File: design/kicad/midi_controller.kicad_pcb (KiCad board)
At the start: 4 copper layers, 166 x 166 mm, 30 parts, among them J1 Conn_01x02_Socket, J2 Conn_01x02_Socket, J3 Conn_01x02_Socket, J4 Conn_01x02_Socket, J5 Conn_01x02_Socket, J6 Conn_01x02_Socket, J7 Conn_01x05, U1 CD74HC4067M

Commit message: Add schematic for MIDI Display MSP2807 with associated components
- Created a new schematic file for the MIDI Display MSP2807.
- Included a unpolarized capacitor (C2) with a value of 100nF.
- Added properties such as reference, value, footprint, and datasheet for the capacitor.
- Integrated the MIDI Display module with detailed pin configurations and properties.
- Defined hierarchical labels for power and data connections (VCC, GND, CS, RST, DC, etc.).
- Ensured all components are marked for BOM inclusion and simulation.
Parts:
- added C5: 10u, Capacitor_SMD:C_0805_2012Metric, F.Cu at (149.9, 21.6)
- added C6: 100n, Capacitor_SMD:C_0603_1608Metric, F.Cu at (154.2, 21.4)
- added C7: 100n, Capacitor_SMD:C_0603_1608Metric, F.Cu at (154.2, 23.9)
- added C8: 10u, Capacitor_SMD:C_0805_2012Metric, F.Cu at (149.9, 24.6)
- added D10: PESD5V0L1BA,115, KiCad:SOD2512X110N, F.Cu at (125.6, 46.6)
- added D11: PESD5V0L1BA,115, KiCad:SOD2512X110N, F.Cu at (125.6, 50.0)
- added D12: PESD5V0L1BA,115, KiCad:SOD2512X110N, F.Cu at (125.6, 53.3)
- added D13: PESD5V0L1BA,115, KiCad:SOD2512X110N, F.Cu at (132.6, 34.6)
- added D14: PESD5V0L1BA,115, KiCad:SOD2512X110N, F.Cu at (132.6, 37.9)
- added D15: PESD5V0L1BA,115, KiCad:SOD2512X110N, F.Cu at (132.6, 41.3)
- added D16: PESD5V0L1BA,115, KiCad:SOD2512X110N, F.Cu at (139.6, 34.6)
- added D17: PESD5V0L1BA,115, KiCad:SOD2512X110N, F.Cu at (139.6, 37.9)
- added D18: PESD5V0L1BA,115, KiCad:SOD2512X110N, F.Cu at (139.6, 41.3)
- added D19: PESD5V0L1BA,115, KiCad:SOD2512X110N, F.Cu at (142.7, 20.5)
- added D2: SS34, Diode_SMD:D_SMA, F.Cu at (127.1, 12.7)
- added D20: PESD5V0L1BA,115, KiCad:SOD2512X110N, F.Cu at (142.7, 23.9)
- added D21: PESD5V0L1BA,115, KiCad:SOD2512X110N, F.Cu at (142.7, 27.2)
- added D22: PESD5V0L1BA,115, KiCad:SOD2512X110N, F.Cu at (125.6, 34.6)
- added D23: PESD5V0L1BA,115, KiCad:SOD2512X110N, F.Cu at (125.6, 37.9)
- added D24: PESD5V0L1BA,115, KiCad:SOD2512X110N, F.Cu at (125.6, 41.3)
- added D25: PESD5V0L1BA,115, KiCad:SOD2512X110N, F.Cu at (139.6, 46.6)
- added D26: PESD5V0L1BA,115, KiCad:SOD2512X110N, F.Cu at (139.6, 50.0)
- added D27: PESD5V0L1BA,115, KiCad:SOD2512X110N, F.Cu at (139.6, 53.3)
- added D28: PESD5V0L1BA,115, KiCad:SOD2512X110N, F.Cu at (118.6, 42.6)
- added D29: PESD5V0L1BA,115, KiCad:SOD2512X110N, F.Cu at (118.6, 46.0)
- added D3: SMAJ5.0CA, Diode_SMD:D_SMA, F.Cu at (135.6, 7.11)
- added D30: PESD5V0L1BA,115, KiCad:SOD2512X110N, F.Cu at (118.6, 49.3)
- added D31: PESD5V0L1BA,115, KiCad:SOD2512X110N, F.Cu at (118.6, 20.5)
- added D32: PESD5V0L1BA,115, KiCad:SOD2512X110N, F.Cu at (118.6, 23.9)
- added D33: PESD5V0L1BA,115, KiCad:SOD2512X110N, F.Cu at (118.6, 27.2)
- added D34: PESD5V0L1BA,115, KiCad:SOD2512X110N, F.Cu at (118.6, 30.6)
- added D35: PESD5V0L1BA,115, KiCad:SOD2512X110N, F.Cu at (118.6, 33.9)
- added D36: PESD5V0L1BA,115, KiCad:SOD2512X110N, F.Cu at (118.6, 37.3)
- added D37: PESD5V0L1BA,115, KiCad:SOD2512X110N, F.Cu at (150.7, 32.6)
- added D38: PESD5V0L1BA,115, KiCad:SOD2512X110N, F.Cu at (150.7, 36.0)
- added D39: PESD5V0L1BA,115, KiCad:SOD2512X110N, F.Cu at (150.7, 39.3)
- added D4: PESD5V0L1BA,115, KiCad:SOD2512X110N, F.Cu at (132.6, 46.6)
- added D40: PESD5V0L1BA,115, KiCad:SOD2512X110N, F.Cu at (150.7, 42.7)
- added D5: PESD5V0L1BA,115, KiCad:SOD2512X110N, F.Cu at (132.6, 50.0)
- added D6: PESD5V0L1BA,115, KiCad:SOD2512X110N, F.Cu at (132.6, 53.3)
- added D7: PESD5V0L1BA,115, KiCad:SOD2512X110N, F.Cu at (135.7, 20.5)
- added D8: PESD5V0L1BA,115, KiCad:SOD2512X110N, F.Cu at (135.7, 23.9)
- added D9: PESD5V0L1BA,115, KiCad:SOD2512X110N, F.Cu at (135.7, 27.2)
- added F1: Fuse, Fuse:Fuse_0805_2012Metric, F.Cu at (125.3, 29.4)
- C1: renamed from C2; footprint Capacitor_SMD:C_0805_2012Metric -> Capacitor_SMD:C_0603_1608Metric
- renumbered C1 to C2, J7 to J1, J1 to J2, J2 to J3, J3 to J4, J4 to J5, J5 to J6, J6 to J7
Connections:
- MCU1 pad 48: +5V -> Net-(MCU1-VIN)

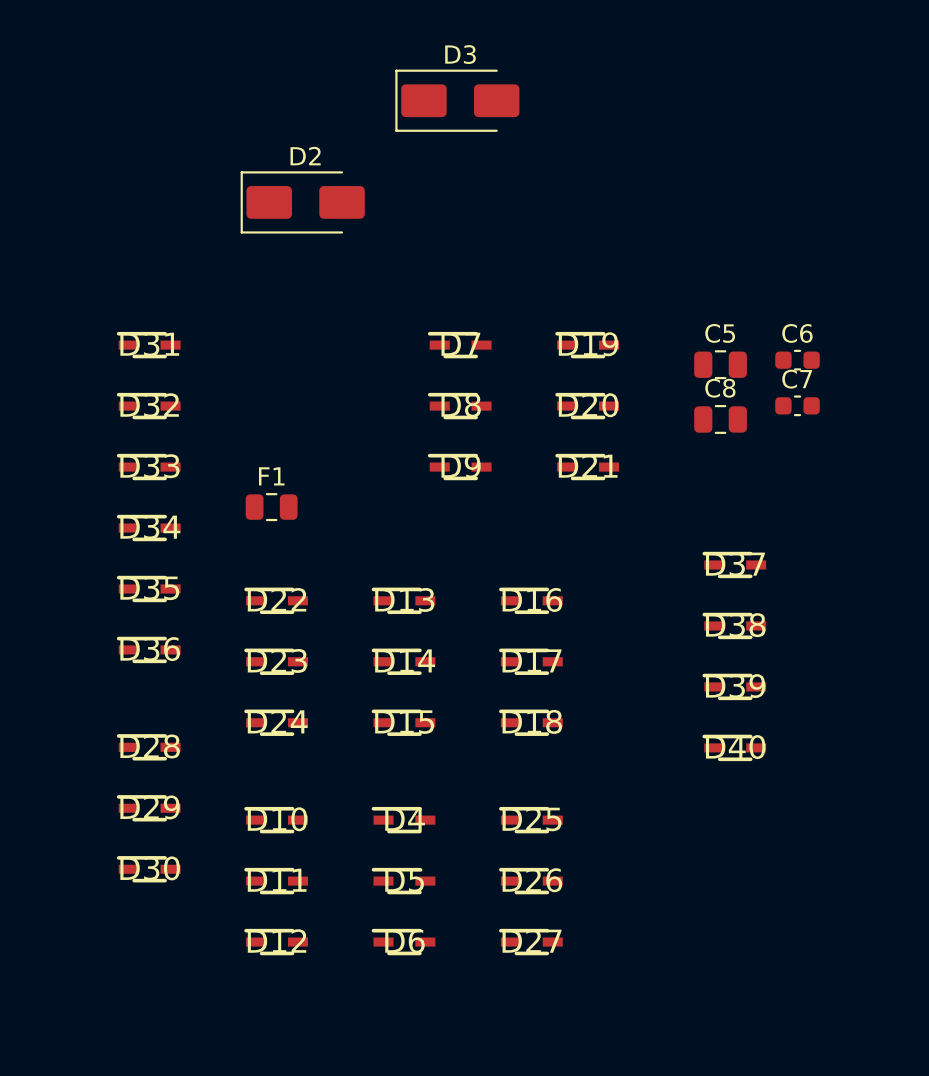
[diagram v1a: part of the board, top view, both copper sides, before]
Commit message: Fix reference labels and update wire connections in MIDI controller and multiplexer schematics
- Adjusted wire connection points in the MIDI controller schematic for better alignment.
- Updated label positions for various components in the MIDI controller schematic.
- Renamed reference designators for capacitors and power connections in the multiplexer schematic to maintain consistency.
- Corrected the reference designators for multiple components to reflect accurate labeling.
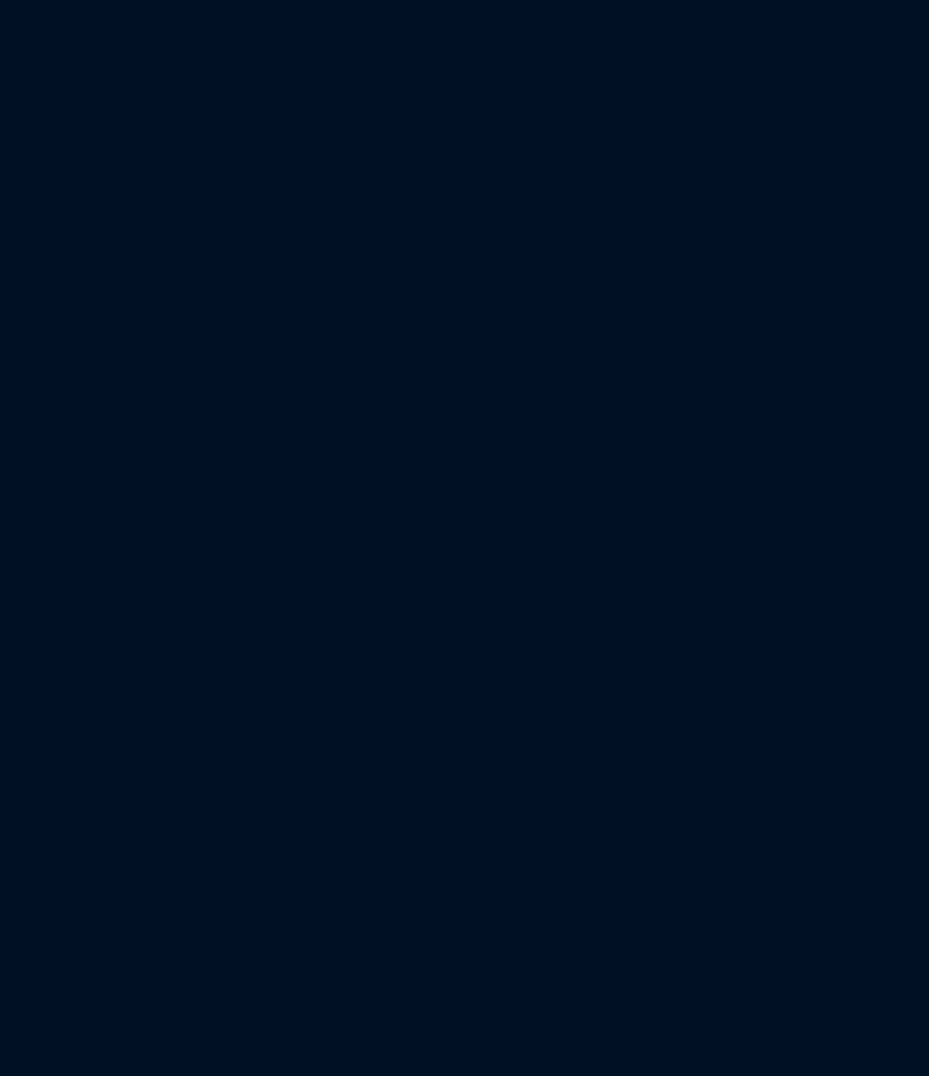
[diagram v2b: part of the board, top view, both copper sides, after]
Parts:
- removed C5, C8: 10u, Capacitor_SMD:C_0805_2012Metric
- removed C6, C7: 100n, Capacitor_SMD:C_0603_1608Metric
- removed D10, D11, D12, D13, D14, D15, D16, D17, D18, D19, D20, D21, D22, D23, D24, D25, D26, D27, D28, D29, D30, D31, D32, D33, D34, D35, D36, D37, D38, D39, D4, D40, D5, D6, D7, D8, D9: PESD5V0L1BA,115, KiCad:SOD2512X110N
- removed D2: SS34, Diode_SMD:D_SMA
- removed D3: SMAJ5.0CA, Diode_SMD:D_SMA
- removed F1: Fuse, Fuse:Fuse_0805_2012Metric

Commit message: Update kicad binary files
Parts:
- added C1: 100p, Capacitor_SMD:C_0603_1608Metric, F.Cu at (33.7, -58.7)
- added C10: 47u, Capacitor_SMD:C_1206_3216Metric, F.Cu at (51.1, -58.3)
- added C11: 47u, Capacitor_SMD:C_1206_3216Metric, F.Cu at (51.1, -54.9)
- added C12: 100u, Capacitor_SMD:C_1210_3225Metric, F.Cu at (39.0, -45.3)
- added C13: 100n, Capacitor_SMD:C_0603_1608Metric, F.Cu at (62.9, -22.5)
- added C14: 100n, Capacitor_SMD:C_0603_1608Metric, F.Cu at (62.9, -20.0)
- added C15: 100n, Capacitor_SMD:C_0603_1608Metric, F.Cu at (62.9, -17.5)
- added C16: 100n, Capacitor_SMD:C_0603_1608Metric, F.Cu at (45.7, -21.2)
- added C17: 100n, Capacitor_SMD:C_0603_1608Metric, F.Cu at (45.7, -18.7)
- added C18: 100n, Capacitor_SMD:C_0603_1608Metric, F.Cu at (45.7, -16.2)
- added C19: 100n, Capacitor_SMD:C_0603_1608Metric, F.Cu at (62.9, -46.6)
- added C2: 10u, Capacitor_SMD:C_0805_2012Metric, F.Cu at (33.9, -45.9)
- added C20: 100n, Capacitor_SMD:C_0603_1608Metric, F.Cu at (62.9, -44.1)
- added C21: 100n, Capacitor_SMD:C_0603_1608Metric, F.Cu at (62.9, -41.6)
- added C22: 100n, Capacitor_SMD:C_0603_1608Metric, F.Cu at (73.9, -46.6)
- added C23: 100n, Capacitor_SMD:C_0603_1608Metric, F.Cu at (73.9, -44.1)
- added C24: 100n, Capacitor_SMD:C_0603_1608Metric, F.Cu at (73.9, -41.6)
- added C25: 100n, Capacitor_SMD:C_0603_1608Metric, F.Cu at (62.9, -34.6)
- added C26: 100n, Capacitor_SMD:C_0603_1608Metric, F.Cu at (62.9, -32.1)
- added C27: 100n, Capacitor_SMD:C_0603_1608Metric, F.Cu at (62.9, -29.6)
- added C28: 100n, Capacitor_SMD:C_0603_1608Metric, F.Cu at (62.9, -58.7)
- added C29: 100n, Capacitor_SMD:C_0603_1608Metric, F.Cu at (62.9, -56.2)
- added C3: 100n, Capacitor_SMD:C_0603_1608Metric, F.Cu at (33.7, -56.2)
- added C30: 100n, Capacitor_SMD:C_0603_1608Metric, F.Cu at (62.9, -53.7)
- added C31: 100n, Capacitor_SMD:C_0603_1608Metric, F.Cu at (73.9, -58.7)
- added C32: 100n, Capacitor_SMD:C_0603_1608Metric, F.Cu at (73.9, -56.2)
- added C33: 100n, Capacitor_SMD:C_0603_1608Metric, F.Cu at (73.9, -53.7)
- added C34: 100n, Capacitor_SMD:C_0603_1608Metric, F.Cu at (73.9, -34.6)
- added C35: 100n, Capacitor_SMD:C_0603_1608Metric, F.Cu at (73.9, -32.1)
- added C36: 100n, Capacitor_SMD:C_0603_1608Metric, F.Cu at (73.9, -29.6)
- added C37: 100n, Capacitor_SMD:C_0603_1608Metric, F.Cu at (73.9, -22.5)
- added C38: 100n, Capacitor_SMD:C_0603_1608Metric, F.Cu at (73.9, -20.0)
- added C39: 100n, Capacitor_SMD:C_0603_1608Metric, F.Cu at (73.9, -17.5)
- added C41: 10uF_0805_16V_lowESR, Capacitor_SMD:C_0805_2012Metric, F.Cu at (80.2, -22.3)
- added C43: 10u, Capacitor_SMD:C_0805_2012Metric, F.Cu at (45.9, -36.3)
- added C5: 1n, Capacitor_SMD:C_0603_1608Metric, F.Cu at (33.7, -53.7)
- added C6: 10n, Capacitor_SMD:C_0603_1608Metric, F.Cu at (33.7, -51.2)
- added C7: 1n, Capacitor_SMD:C_0603_1608Metric, F.Cu at (33.7, -48.7)
- added C9: 100n, Capacitor_SMD:C_0805_2012Metric, F.Cu at (33.9, -42.9)
- added D1: SS34, Diode_SMD:D_SMA, F.Cu at (47.8, -46.7)
- added D10: PESD5V0L1BA,115, KiCad:SOD2512X110N, F.Cu at (58.4, -42.9)
- added D11: PESD5V0L1BA,115, KiCad:SOD2512X110N, F.Cu at (58.4, -39.5)
- added D12: PESD5V0L1BA,115, KiCad:SOD2512X110N, F.Cu at (69.4, -46.2)
- added D13: PESD5V0L1BA,115, KiCad:SOD2512X110N, F.Cu at (69.4, -42.9)
- added D14: PESD5V0L1BA,115, KiCad:SOD2512X110N, F.Cu at (69.4, -39.5)
- added D15: PESD5V0L1BA,115, KiCad:SOD2512X110N, F.Cu at (58.4, -34.2)
- added D16: PESD5V0L1BA,115, KiCad:SOD2512X110N, F.Cu at (58.4, -30.8)
- added D17: PESD5V0L1BA,115, KiCad:SOD2512X110N, F.Cu at (58.4, -27.5)
- added D18: PESD5V0L1BA,115, KiCad:SOD2512X110N, F.Cu at (58.4, -58.3)
- added D19: PESD5V0L1BA,115, KiCad:SOD2512X110N, F.Cu at (58.4, -54.9)
- added D2: SMAJ5.0CA, Diode_SMD:D_SMA, F.Cu at (47.8, -42.1)
- added D20: PESD5V0L1BA,115, KiCad:SOD2512X110N, F.Cu at (58.4, -51.6)
- added D21: PESD5V0L1BA,115, KiCad:SOD2512X110N, F.Cu at (69.4, -58.3)
- added D22: PESD5V0L1BA,115, KiCad:SOD2512X110N, F.Cu at (69.4, -54.9)
- added D23: PESD5V0L1BA,115, KiCad:SOD2512X110N, F.Cu at (69.4, -51.6)
- added D24: PESD5V0L1BA,115, KiCad:SOD2512X110N, F.Cu at (69.4, -34.2)
- added D25: PESD5V0L1BA,115, KiCad:SOD2512X110N, F.Cu at (69.4, -30.8)
- added D26: PESD5V0L1BA,115, KiCad:SOD2512X110N, F.Cu at (69.4, -27.5)
- added D27: PESD5V0L1BA,115, KiCad:SOD2512X110N, F.Cu at (69.4, -22.1)
- added D28: PESD5V0L1BA,115, KiCad:SOD2512X110N, F.Cu at (69.4, -18.8)
- added D29: PESD5V0L1BA,115, KiCad:SOD2512X110N, F.Cu at (69.4, -15.4)
- added D3: PESD5V0L1BA,115, KiCad:SOD2512X110N, F.Cu at (58.4, -22.1)
- added D30: PESD5V0L1BA,115, KiCad:SOD2512X110N, F.Cu at (34.2, -36.2)
- added D31: PESD5V0L1BA,115, KiCad:SOD2512X110N, F.Cu at (34.2, -32.8)
- added D32: PESD5V0L1BA,115, KiCad:SOD2512X110N, F.Cu at (34.2, -29.5)
- added D33: PESD5V0L1BA,115, KiCad:SOD2512X110N, F.Cu at (34.2, -26.1)
- added D34: PESD5V0L1BA,115, KiCad:SOD2512X110N, F.Cu at (34.2, -22.8)
- added D35: PESD5V0L1BA,115, KiCad:SOD2512X110N, F.Cu at (34.2, -19.4)
- added D36: PESD5V0L1BA,115, KiCad:SOD2512X110N, F.Cu at (41.2, -36.2)
- added D37: PESD5V0L1BA,115, KiCad:SOD2512X110N, F.Cu at (41.2, -32.8)
- added D38: PESD5V0L1BA,115, KiCad:SOD2512X110N, F.Cu at (41.2, -29.5)
- added D39: PESD5V0L1BA,115, KiCad:SOD2512X110N, F.Cu at (41.2, -26.1)
- added D4: PESD5V0L1BA,115, KiCad:SOD2512X110N, F.Cu at (58.4, -18.8)
- added D5: PESD5V0L1BA,115, KiCad:SOD2512X110N, F.Cu at (58.4, -15.4)
- added D6: PESD5V0L1BA,115, KiCad:SOD2512X110N, F.Cu at (41.2, -20.8)
- added D7: PESD5V0L1BA,115, KiCad:SOD2512X110N, F.Cu at (41.2, -17.4)
- added D8: PESD5V0L1BA,115, KiCad:SOD2512X110N, F.Cu at (41.2, -14.1)
- added D9: PESD5V0L1BA,115, KiCad:SOD2512X110N, F.Cu at (58.4, -46.2)
- added F1: Fuse, Fuse:Fuse_0805_2012Metric, F.Cu at (38.3, -41.7)
- added FB1: FerriteBead, Inductor_SMD:L_0805_2012Metric, F.Cu at (46.0, -58.6)
- added FB2: FerriteBead, Inductor_SMD:L_0805_2012Metric, F.Cu at (46.0, -55.8)
- added FB3: FerriteBead, Inductor_SMD:L_0805_2012Metric, F.Cu at (46.0, -53.1)
- added FB4: FerriteBead, Inductor_SMD:L_0805_2012Metric, F.Cu at (46.0, -50.3)
- added J9: Conn_01x14, Connector_PinSocket_2.54mm:PinSocket_1x14_P2.54mm_Vertical, F.Cu at (113.8, 91.0)
- added R1: 220, Resistor_SMD:R_0603_1608Metric, F.Cu at (37.7, -58.7)
- added R2: 100, Resistor_SMD:R_0603_1608Metric, F.Cu at (37.7, -56.2)
- added R3: 100, Resistor_SMD:R_0603_1608Metric, F.Cu at (37.7, -53.7)
- added R4: 100, Resistor_SMD:R_0603_1608Metric, F.Cu at (37.7, -51.2)
- added R5: 33, Resistor_SMD:R_0603_1608Metric, F.Cu at (37.7, -48.7)
- added R6: 33, Resistor_SMD:R_0603_1608Metric, F.Cu at (41.7, -58.7)
- added R7: 100, Resistor_SMD:R_0603_1608Metric, F.Cu at (41.7, -56.2)
- added R8: 33, Resistor_SMD:R_0603_1608Metric, F.Cu at (41.7, -53.7)
- added R9: 33, Resistor_SMD:R_0603_1608Metric, F.Cu at (41.7, -51.2)
- C42: renamed from C4; footprint Capacitor_SMD:C_0805_2012Metric -> Capacitor_SMD:C_0603_1608Metric
- renumbered C1 to C4, C2 to C40, C3 to C8, D1 to DISP1
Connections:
- net /Encoder with Push Button_Navigation/QUAD_A renamed /Encoder_with_Push_Button_Navigation/QUAD_A
- net /Encoder with Push Button_Navigation/QUAD_B renamed /Encoder_with_Push_Button_Navigation/QUAD_B
- net /Encoder with Push Button_Navigation/SW_A renamed /Encoder_with_Push_Button_Navigation/SW_A
- net Net-(D1-RST) renamed /RST
- net Net-(D1-SDO/MISO) renamed /MISO
- C4 pad 1: +3V3 -> Net-(C4-Pad1)
- DISP1 pad 3: Net-(D1-CS) -> /CS
- DISP1 pad 5: Net-(D1-DC) -> /DC
- DISP1 pad 6: Net-(D1-SDI/MOSI) -> /MOSI
- DISP1 pad 7: Net-(D1-SCK) -> /Display MSP2807/SCK
- DISP1 pad 8: +3V3 -> /Display MSP2807/LED
- J1 pad 1: +5V -> Net-(J1-Pin_1)
- MCU1 pad 18: Net-(D1-SDI/MOSI) -> Net-(MCU1-26_A12_MOSI1)
- MCU1 pad 19: Net-(D1-SCK) -> Net-(MCU1-27_A13_SCK1)
- MCU1 pad 2: Net-(D1-DC) -> Net-(MCU1-0_RX1_CRX2_CS1)
- MCU1 pad 20: Net-(D1-CS) -> Net-(MCU1-28_RX7)
- MCU1 pad 46: +3V3 -> Net-(C4-Pad1)
- MCU1 pad 5: /S0 -> Net-(MCU1-3_LRCLK2)
- MCU1 pad 6: /S1 -> Net-(MCU1-4_BCLK2)
- MCU1 pad 7: /S2 -> Net-(MCU1-5_IN2)
- MCU1 pad 8: /S3 -> Net-(MCU1-6_OUT1D)
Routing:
- net (no net): track 0.00 -> 225.4 mm
- net Net-(D1-CS): track 70.9 -> 0.00 mm
- net Net-(D1-SCK): track 68.3 -> 0.00 mm
- net Net-(D1-SDI/MOSI): track 64.0 -> 0.00 mm
- net Net-(D1-DC): track 22.3 -> 0.00 mm

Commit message: Update kicad binary files
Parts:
- removed MCU1: MIDI_Teensy4.1, midi_controller:Teensy41
- added J10: Conn_01x24_Socket, Connector_PinSocket_2.54mm:PinSocket_1x24_P2.54mm_Vertical, B.Cu at (133.0, 115.1)
- D36, D37, D38, D39, R2, R3, R4, R7: moved to B.Cu
- J9: value Conn_01x14 -> Conn_01x24_Socket; footprint Connector_PinSocket_2.54mm:PinSocket_1x14_P2.54mm_Vertical -> Connector_PinSocket_2.54mm:PinSocket_1x24_P2.54mm_Vertical; moved to B.Cu
- moved FB4 269.9 mm to (213.9, 161.0), turned to 180 degrees
- moved C1 218.5 mm to (180.2, 103.4), turned to 90 degrees
- moved FB1 210.1 mm to (177.7, 105.2)
- moved R8 207.8 mm to (178.7, 102.6), turned to 90 degrees
- moved R5 205.1 mm to (176.2, 102.6), turned to 90 degrees
- moved FB3 203.7 mm to (59.8, 150.2)
- moved C11 203.7 mm to (64.9, 148.3)
- moved R9 203.6 mm to (181.3, 97.0), turned to -90 degrees
- moved C5 202.3 mm to (153.5, 109.4), turned to -90 degrees
- moved C6 199.5 mm to (152.0, 109.4), turned to -90 degrees
- moved C2 198.3 mm to (69.9, 149.1)
- moved C7 198.3 mm to (69.6, 146.4)
- moved C9 198.3 mm to (69.9, 152.1)
- moved C3 195.7 mm to (75.1, 135.1)
- moved R7 193.1 mm to (150.8, 103.1), turned to -90 degrees
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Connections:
- C4 pad 1: Net-(C4-Pad1) -> +3V3
- F1 pad 1: Net-(MCU1-VIN) -> +5V
- FB3 pad 1: Net-(C4-Pad1) -> +3V3
- J9 pad 1: +5V -> GND
- J9 pad 10: unconnected-(J9-Pin_10-Pad10) -> /Teensy_4.1/T8
- J9 pad 11: unconnected-(J9-Pin_11-Pad11) -> /Teensy_4.1/T9
- J9 pad 12: unconnected-(J9-Pin_12-Pad12) -> /Teensy_4.1/T10
- J9 pad 13: unconnected-(J9-Pin_13-Pad13) -> /Teensy_4.1/T11
- J9 pad 14: unconnected-(J9-Pin_14-Pad14) -> /Teensy_4.1/T12
- J9 pad 2: GND -> /Teensy_4.1/T0
- J9 pad 3: /CS -> /MISO
- J9 pad 4: /RST -> /COM
- J9 pad 5: /DC -> /Teensy_4.1/T3
- J9 pad 6: /MOSI -> /Teensy_4.1/T4
- J9 pad 7: /Display MSP2807/SCK -> /Teensy_4.1/T5
- J9 pad 8: /Display MSP2807/LED -> /Teensy_4.1/T6
- J9 pad 9: /MISO -> /Teensy_4.1/T7
- R2 pad 1: Net-(MCU1-3_LRCLK2) -> /Teensy_4.1/T3
- R3 pad 1: Net-(MCU1-4_BCLK2) -> /Teensy_4.1/T4
- R4 pad 1: Net-(MCU1-5_IN2) -> /Teensy_4.1/T5
- R5 pad 2: Net-(MCU1-26_A12_MOSI1) -> /Teensy_4.1/T26
- R6 pad 2: Net-(MCU1-0_RX1_CRX2_CS1) -> /Teensy_4.1/T0
- R7 pad 1: Net-(MCU1-6_OUT1D) -> /Teensy_4.1/T6
- R8 pad 2: Net-(MCU1-27_A13_SCK1) -> /Teensy_4.1/T27
- R9 pad 2: Net-(MCU1-28_RX7) -> /Teensy_4.1/T28
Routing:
- net (no net): track 225.4 -> 0.00 mm
- net /CS: track 0.00 -> 68.2 mm
- net /Display MSP2807/SCK: track 0.00 -> 64.6 mm
- net /MOSI: track 0.00 -> 63.2 mm
- net /DC: track 0.00 -> 23.6 mm
- net GND: track 13.6 -> 33.5 mm, vias 4 -> 9
- net +5V: track 167.3 -> 177.0 mm, vias 1 -> 3
- net /Buttons_Momentary/BUTTON_PUSH_MOM_04: track 95.2 -> 99.9 mm
- net Net-(D1-K): track 0.00 -> 3.96 mm
- net /SCK: track 0.00 -> 3.78 mm
- net +3V3: track 110.1 -> 106.3 mm, vias 3 -> 4
- net Net-(J1-Pin_1): track 0.00 -> 2.53 mm
- net /Teensy_4.1/T3: track 0.00 -> 2.53 mm
- net /Teensy_4.1/T5: track 0.00 -> 2.46 mm
- net /Teensy_4.1/T4: track 0.00 -> 2.44 mm
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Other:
- outline, holes or cut-outs redrawn
